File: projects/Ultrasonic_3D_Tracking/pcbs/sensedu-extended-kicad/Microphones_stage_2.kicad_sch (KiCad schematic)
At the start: 36 parts, among them U10 AD8426ACPZ-R7, U9 AD8426ACPZ-R7

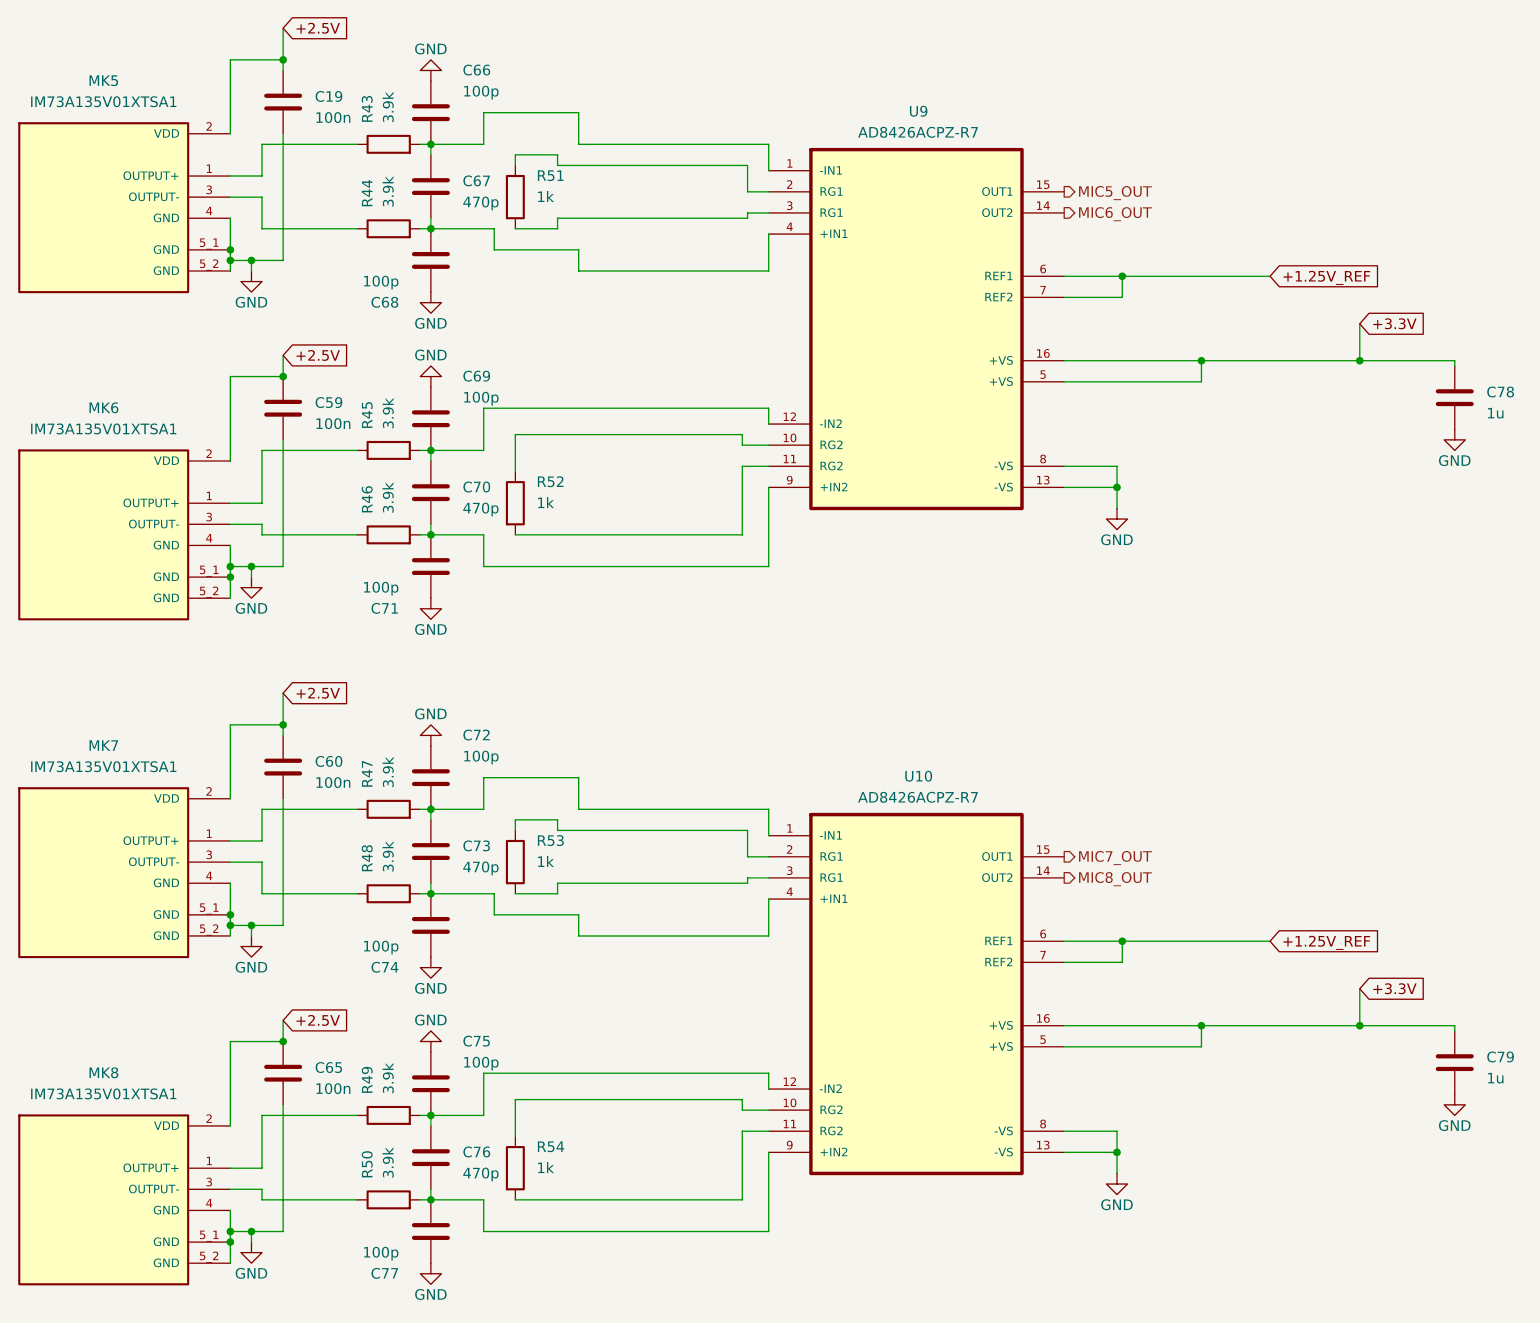
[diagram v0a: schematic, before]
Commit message: Fix: Cleaned schematic
- project is not correctly set up, so cannot be ordered without further
   work
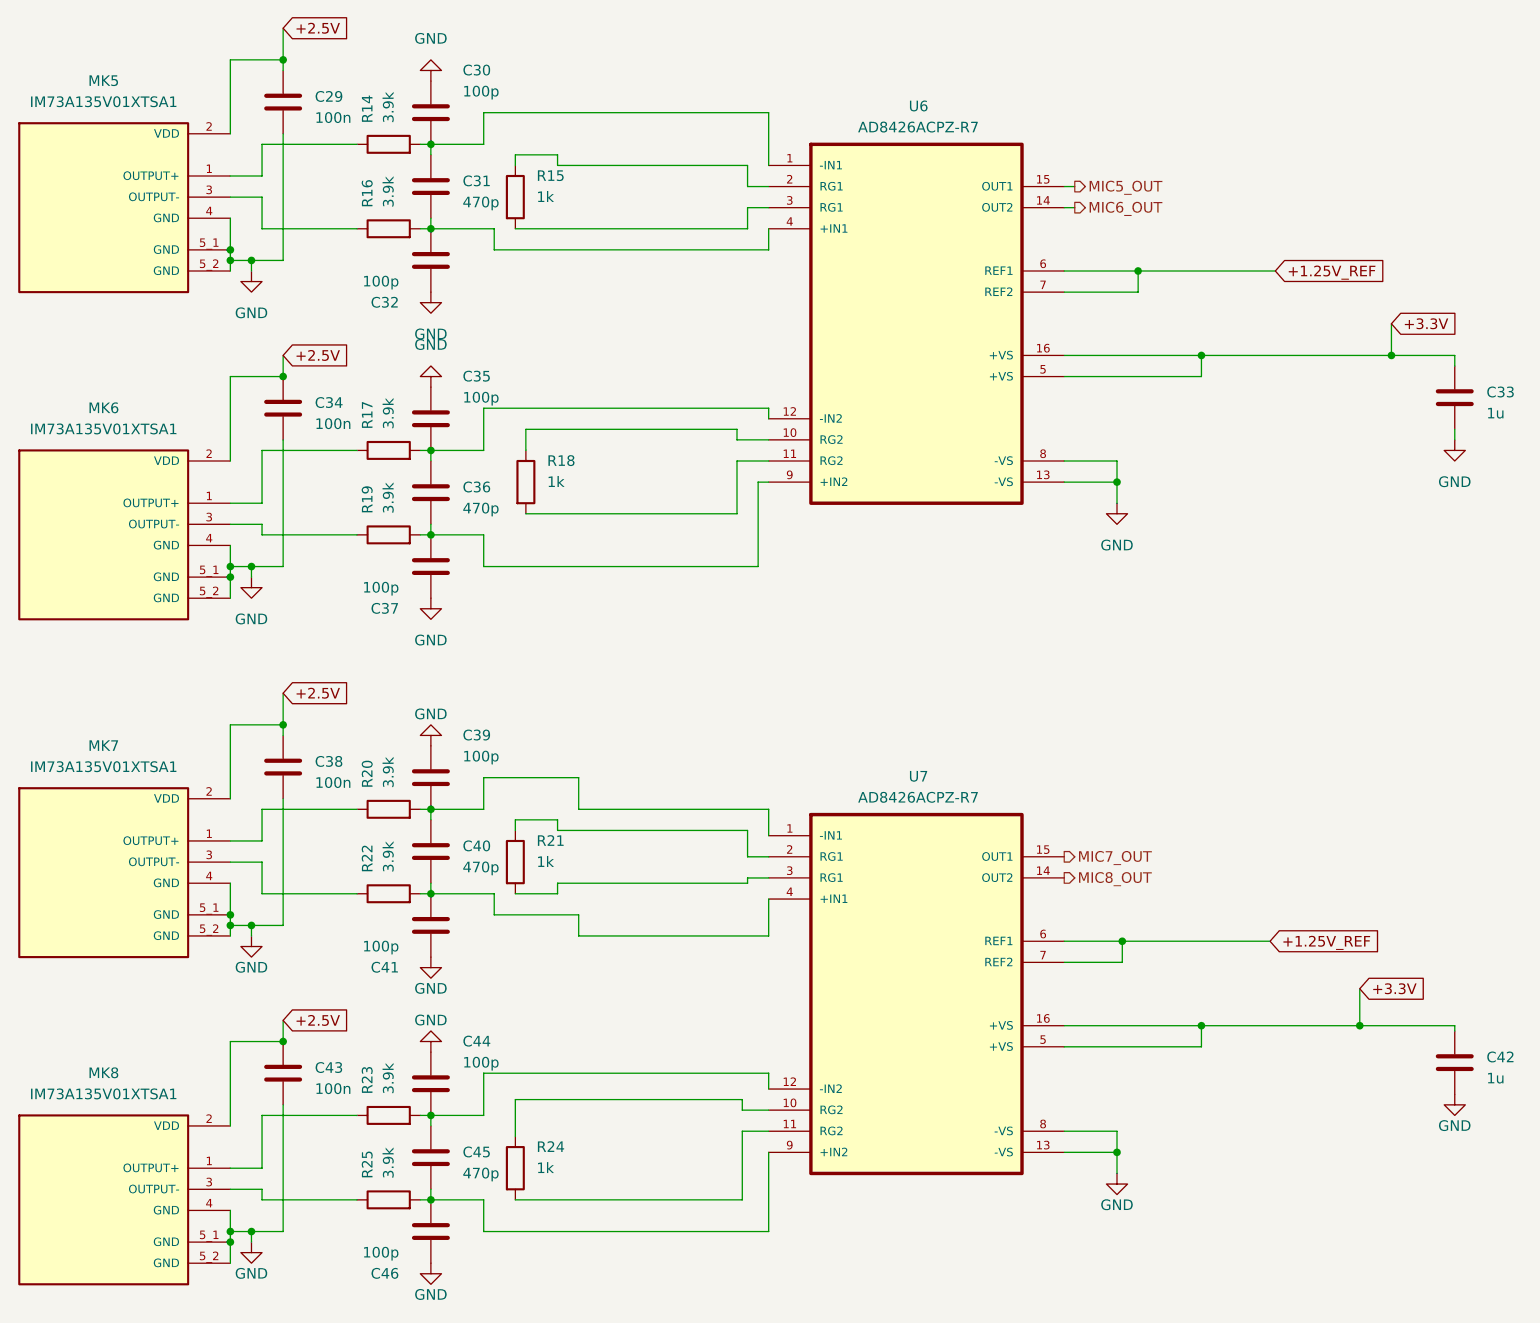
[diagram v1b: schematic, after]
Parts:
- renumbered C19 to C29, C66 to C30, C67 to C31, C68 to C32, C78 to C33, C59 to C34, C69 to C35, C70 to C36, C71 to C37, C60 to C38, C72 to C39, C73 to C40, C74 to C41, C79 to C42, C65 to C43, C75 to C44, C76 to C45, C77 to C46, R43 to R14, R51 to R15, R44 to R16, R45 to R17, R52 to R18, R46 to R19, R47 to R20, R53 to R21, R48 to R22, R49 to R23, R54 to R24, R50 to R25, U9 to U6, U10 to U7
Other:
- moved on the sheet: R18, U6
